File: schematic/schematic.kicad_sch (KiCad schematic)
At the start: 82 parts, among them J1 GATE_OUT_1, J10 CV_OUT_2, J11 FWD_CLK_IN, J12 BWD_CLK_IN, J13 RST_IN, J14 KBD_Gate_Out, J2 GATE_OUT_2, J3 GATE_OUT_3, J4 GATE_OUT_4, J5 GATE_OUT_5, J6 GATE_OUT_6, J7 GATE_OUT_7, J8 GATE_OUT_8, J9 CV_OUT_1, SW1 BUTTON_2, SW10 FWD_BWD_SWITCH, SW2 BUTTON_2, SW3 BUTTON_3, SW4 BUTTON_4, SW5 BUTTON_5, SW6 BUTTON_6, SW7 BUTTON_7, SW8 BUTTON_8, SW9 RESET_ZERO_SW, U1 L78L05_TO92

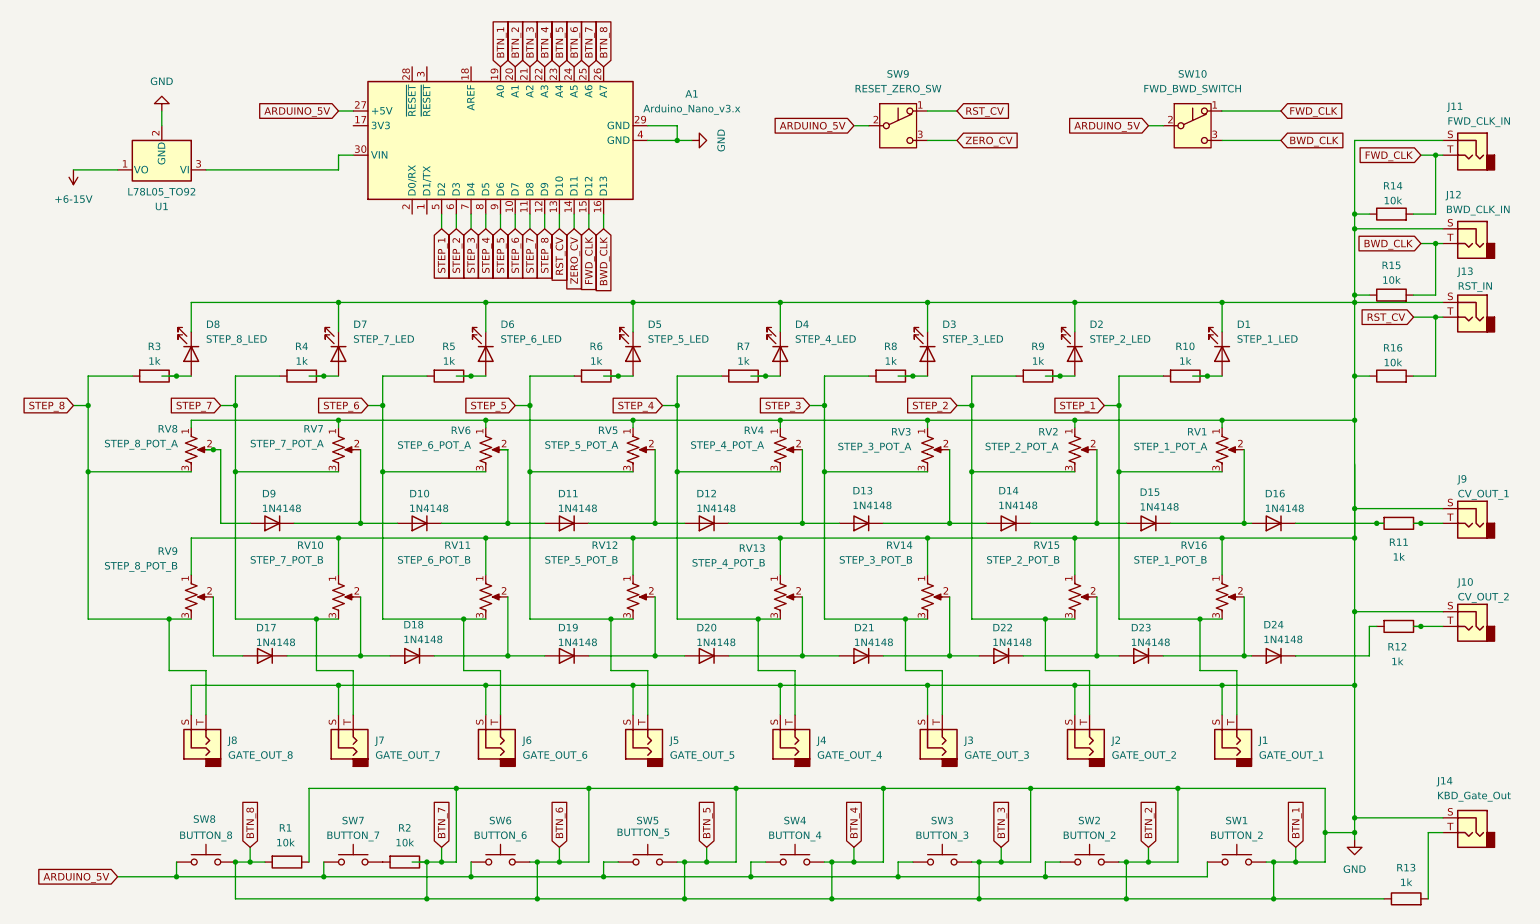
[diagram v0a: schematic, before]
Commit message: Bug fixes and refactor, + update README
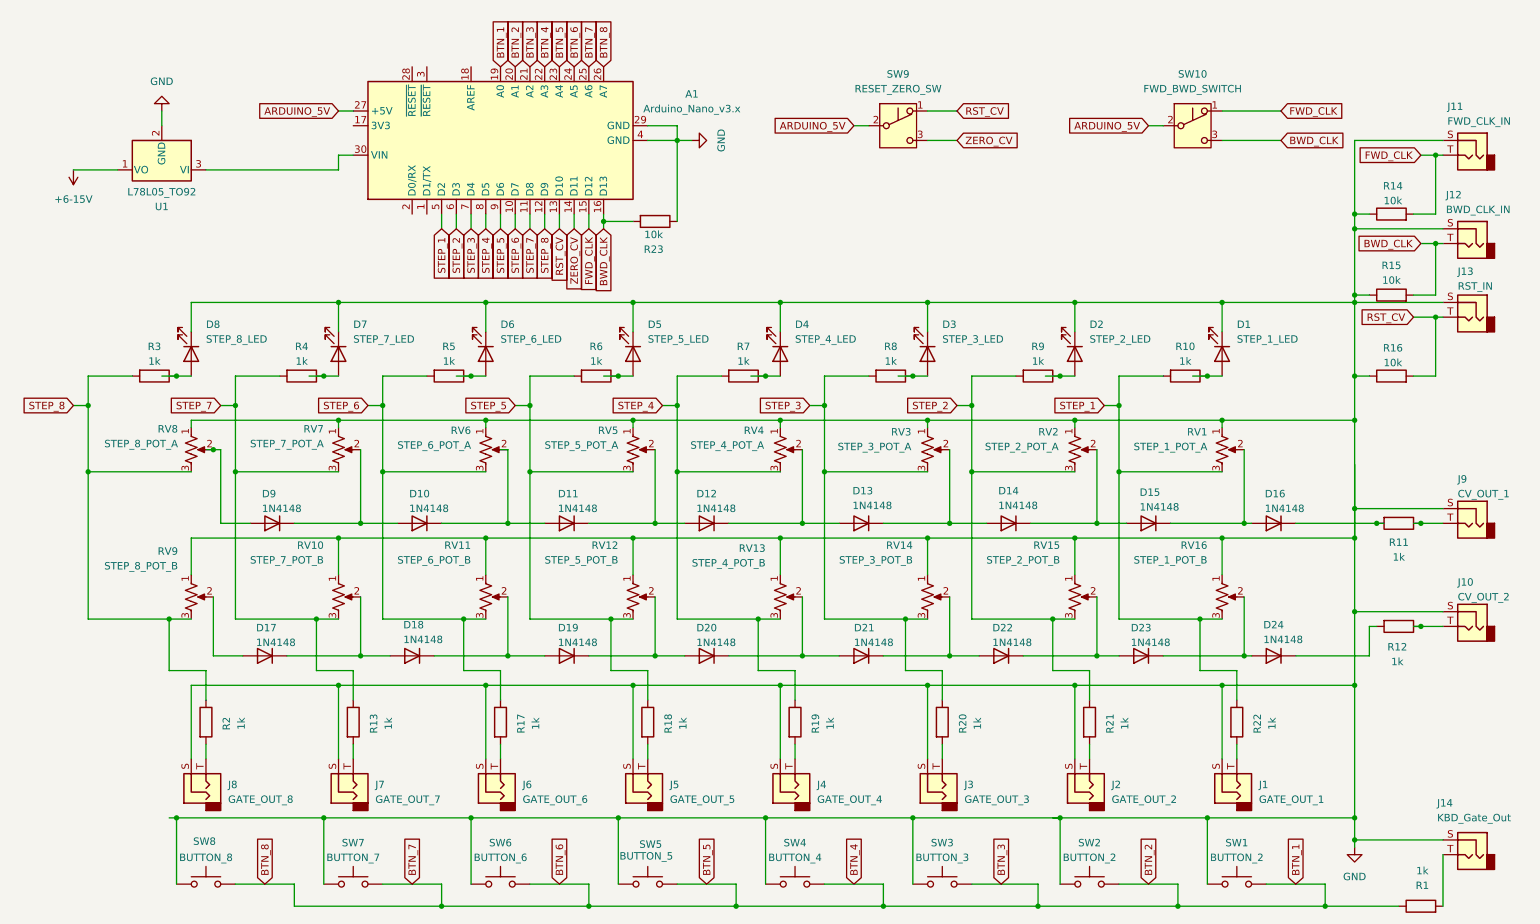
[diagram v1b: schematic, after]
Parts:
- added R17, R18, R19, R20, R21, R22: 1k, symbol Device:R
- added R23: 10k, symbol Device:R
- R1, R2: value 10k -> 1k
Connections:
- net ARDUINO_5V: no longer SW1.1, SW2.1, SW3.1, SW4.1, SW5.1, SW6.1, SW7.1, SW8.1
- net BWD_CLK: now also R23.2
- net GND: now also SW1.1, SW2.1, SW3.1, SW4.1, SW5.1, SW6.1, SW7.1, SW8.1, R23.1; no longer A1.19 (A0), A1.20 (A1), A1.21 (A2), A1.22 (A3), A1.23 (A4), A1.24 (A5), A1.25 (A6), A1.26 (A7), R1.1, R1.2, R13.1, R2.1, SW1.2, SW2.2, SW3.2, SW4.2, SW5.2, SW6.2, SW8.2
- net STEP_1: now also R22.1; no longer J1.T
- net STEP_2: now also R21.1; no longer J2.T
- net STEP_3: now also R20.1; no longer J3.T
- net STEP_4: now also R19.1; no longer J4.T
- net STEP_5: now also R18.1; no longer J5.T
- net STEP_6: now also R17.1; no longer J6.T
- net STEP_7: now also R13.1; no longer J7.T
- net STEP_8: now also R2.1; no longer J8.T
- net at R2.2: now also J8.T; no longer SW7.2
- net at R13.2: now also J7.T; no longer J14.T
- new net: J2.T, R21.2
- new net: J5.T, R18.2
- new net: J3.T, R20.2
- new net: J1.T, R22.2
- new net: J4.T, R19.2
- new net: J14.T, R1.2
- new net: J6.T, R17.2
- new net BTN_1: A1.19 (A0), A1.20 (A1), A1.21 (A2), A1.22 (A3), A1.23 (A4), A1.24 (A5), A1.25 (A6), A1.26 (A7), R1.1, SW1.2, SW2.2, SW3.2, SW4.2, SW5.2, SW6.2, SW7.2, SW8.2
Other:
- moved on the sheet: J1, J14, J2, J3, J4, J5, J6, J7, J8, SW1, SW2, SW3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

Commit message: Fix stacked diodes and D13 on schematic
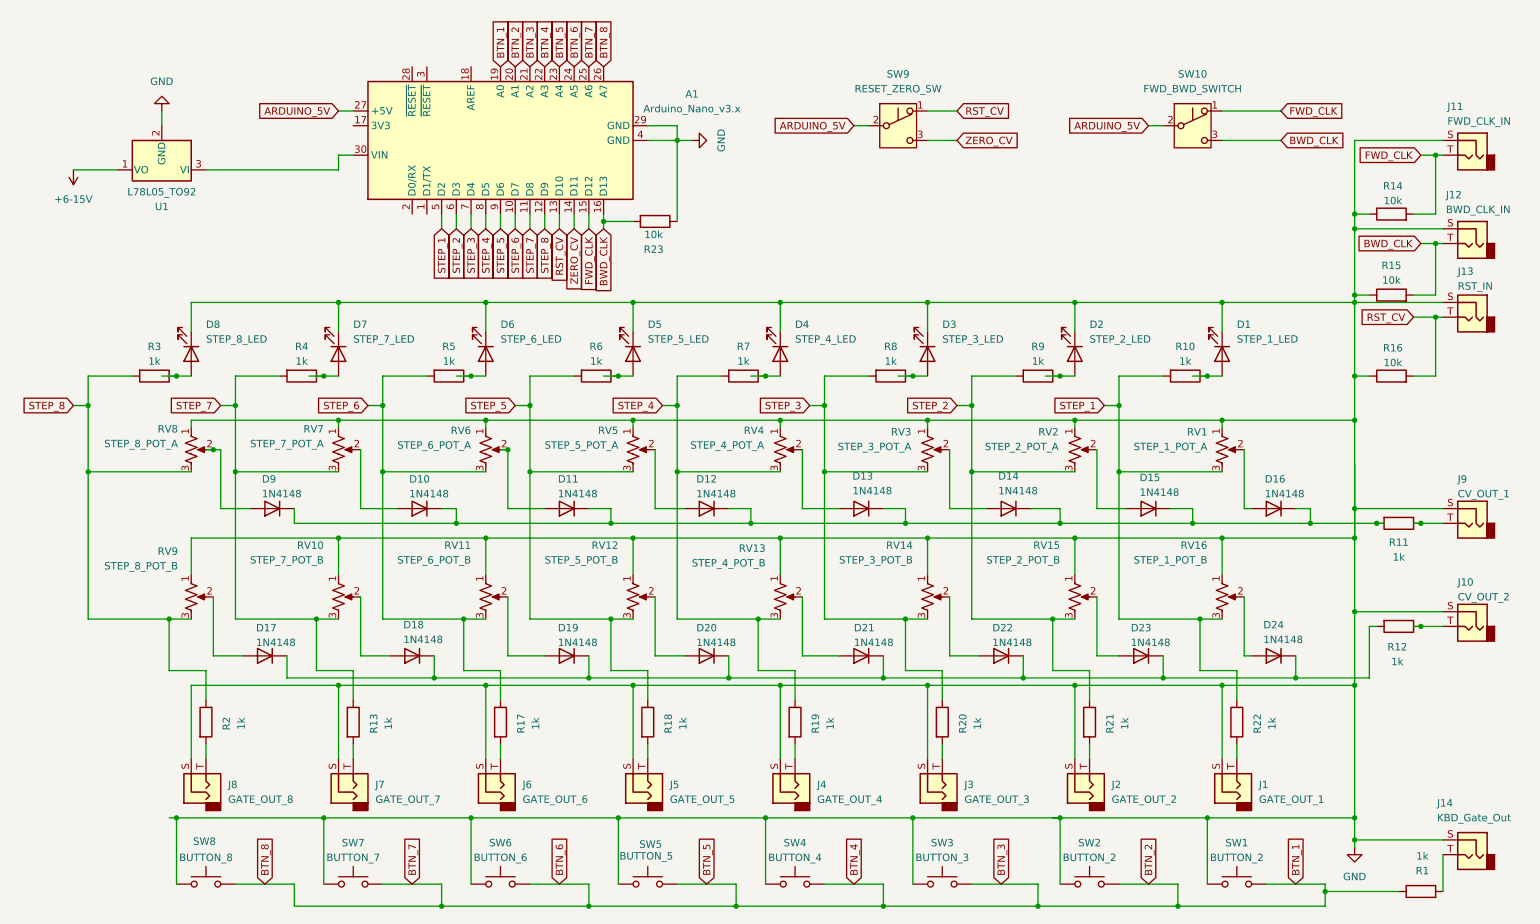
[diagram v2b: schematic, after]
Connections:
- net at D22.2 (A), RV14.2: no longer D21.1 (K)
- net at D21.2 (A), RV13.2: no longer D20.1 (K)
- net at D13.2 (A), RV4.2: no longer D12.1 (K)
- net at D12.2 (A), RV5.2: no longer D11.1 (K)
- net at D20.2 (A), RV12.2: no longer D19.1 (K)
- net at D24.2 (A), RV16.2: no longer D23.1 (K)
- net at D23.2 (A), RV15.2: no longer D22.1 (K)
- net at D11.2 (A), RV6.2: no longer D10.1 (K)
- net at D18.2 (A), RV10.2: no longer D17.1 (K)
- net at D15.2 (A), RV2.2: no longer D14.1 (K)
- net at D14.2 (A), RV3.2: no longer D13.1 (K)
- net at D19.2 (A), RV11.2: no longer D18.1 (K)
- net at D16.2 (A), RV1.2: no longer D15.1 (K)
- net at D16.1 (K), R11.2: now also D10.1 (K), D11.1 (K), D12.1 (K), D13.1 (K), D14.1 (K), D15.1 (K), D9.1 (K)
- net at D24.1 (K), R12.2: now also D17.1 (K), D18.1 (K), D19.1 (K), D20.1 (K), D21.1 (K), D22.1 (K), D23.1 (K)
- net at D10.2 (A), RV7.2: no longer D9.1 (K)
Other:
- moved on the sheet: D10, D11, D12, D13, D14, D15, D16, D9, R1
